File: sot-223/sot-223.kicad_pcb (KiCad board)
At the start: 2 copper layers, 21.6 x 15.2 mm, 2 parts, among them J1 Conn_01x04, J2 Conn_01x04_Male

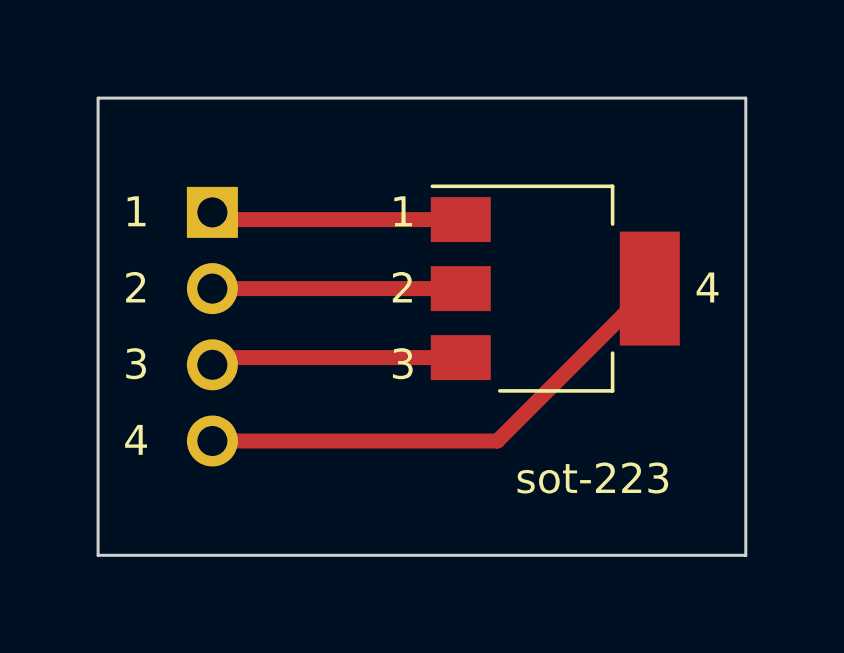
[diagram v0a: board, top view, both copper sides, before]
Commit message: Add zones to SOT-223 PCB
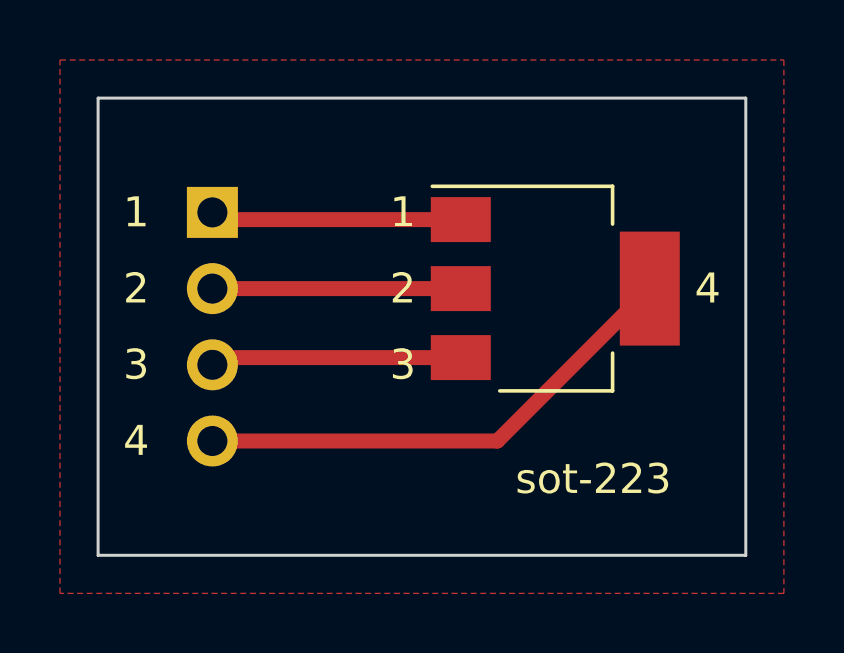
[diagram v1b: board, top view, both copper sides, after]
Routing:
- added copper zone on F.Cu, net (none)
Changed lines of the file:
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@@
       (effects (font (size 1 1) (thickness 0.15)) (justify mirror))
     )
+    (fp_line (start 1.8 1.8) (end -1.8 1.8) (layer B.CrtYd) (width 0.05))
+    (fp_line (start 1.8 -9.4) (end 1.8 1.8) (layer B.CrtYd) (width 0.05))
+    (fp_line (start -1.8 -9.4) (end 1.8 -9.4) (layer B.CrtYd) (width 0.05))
+    (fp_line (start -1.8 1.8) (end -1.8 -9.4) (layer B.CrtYd) (width 0.05))
+    (fp_line (start -1.33 1.33) (end 0 1.33) (layer B.SilkS) (width 0.12))
+    (fp_line (start -1.33 0) (end -1.33 1.33) (layer B.SilkS) (width 0.12))
+    (fp_line (start -1.33 -1.27) (end 1.33 -1.27) (layer B.SilkS) (width 0.12))
+    (fp_line (start 1.33 -1.27) (end 1.33 -8.95) (layer B.SilkS) (width 0.12))
+    (fp_line (start -1.33 -1.27) (end -1.33 -8.95) (layer B.SilkS) (width 0.12))
+    (fp_line (start -1.33 -8.95) (end 1.33 -8.95) (layer B.SilkS) (width 0.12))
+    (fp_line (start -1.27 0.635) (end -0.635 1.27) (layer B.Fab) (width 0.1))
+    (fp_line (start -1.27 -8.89) (end -1.27 0.635) (layer B.Fab) (width 0.1))
+    (fp_line (start 1.27 -8.89) (end -1.27 -8.89) (layer B.Fab) (width 0.1))
+    (fp_line (start 1.27 1.27) (end 1.27 -8.89) (layer B.Fab) (width 0.1))
+    (fp_line (start -0.635 1.27) (end 1.27 1.27) (layer B.Fab) (width 0.1))
     (fp_text user %R (at 0 -3.81 270) (layer B.Fab)
       (effects (font (size 1 1) (thickness 0.15)) (justify mirror))
     )
-    (fp_line (start -0.635 1.27) (end 1.27 1.27) (layer B.Fab) (width 0.1))
-    (fp_line (start 1.27 1.27) (end 1.27 -8.89) (layer B.Fab) (width 0.1))
-    (fp_line (start 1.27 -8.89) (end -1.27 -8.89) (layer B.Fab) (width 0.1))
-    (fp_line (start -1.27 -8.89) (end -1.27 0.635) (layer B.Fab) (width 0.1))
-    (fp_line (start -1.27 0.635) (end -0.635 1.27) (layer B.Fab) (width 0.1))
-    (fp_line (start -1.33 -8.95) (end 1.33 -8.95) (layer B.SilkS) (width 0.12))
-    (fp_line (start -1.33 -1.27) (end -1.33 -8.95) (layer B.SilkS) (width 0.12))
-    (fp_line (start 1.33 -1.27) (end 1.33 -8.95) (layer B.SilkS) (width 0.12))
-    (fp_line (start -1.33 -1.27) (end 1.33 -1.27) (layer B.SilkS) (width 0.12))
-    (fp_line (start -1.33 0) (end -1.33 1.33) (layer B.SilkS) (width 0.12))
-    (fp_line (start -1.33 1.33) (end 0 1.33) (layer B.SilkS) (width 0.12))
-    (fp_line (start -1.8 1.8) (end -1.8 -9.4) (layer B.CrtYd) (width 0.05))
-    (fp_line (start -1.8 -9.4) (end 1.8 -9.4) (layer B.CrtYd) (width 0.05))
-    (fp_line (start 1.8 -9.4) (end 1.8 1.8) (layer B.CrtYd) (width 0.05))
-    (fp_line (start 1.8 1.8) (end -1.8 1.8) (layer B.CrtYd) (width 0.05))
     (pad 4 thru_hole oval (at 0 -7.62 180) (size 1.7 1.7) (drill 1) (layers *.Cu *.Mask)
       (net 4 "Net-(J1-Pad4)"))
@@
       (effects (font (size 1 1) (thickness 0.15)))
     )
+    (fp_line (start 1.85 -3.35) (end 1.85 3.35) (layer F.Fab) (width 0.1))
+    (fp_line (start -1.85 3.35) (end 1.85 3.35) (layer F.Fab) (width 0.1))
+    (fp_line (start -4.1 -3.41) (end 1.91 -3.41) (layer F.SilkS) (width 0.12))
+    (fp_line (start -0.8 -3.35) (end 1.85 -3.35) (layer F.Fab) (width 0.1))
+    (fp_line (start -1.85 3.41) (end 1.91 3.41) (layer F.SilkS) (width 0.12))
+    (fp_line (start -1.85 -2.3) (end -1.85 3.35) (layer F.Fab) (width 0.1))
+    (fp_line (start -4.4 -3.6) (end -4.4 3.6) (layer F.CrtYd) (width 0.05))
+    (fp_line (start -4.4 3.6) (end 4.4 3.6) (layer F.CrtYd) (width 0.05))
+    (fp_line (start 4.4 3.6) (end 4.4 -3.6) (layer F.CrtYd) (width 0.05))
+    (fp_line (start 4.4 -3.6) (end -4.4 -3.6) (layer F.CrtYd) (width 0.05))
+    (fp_line (start 1.91 -3.41) (end 1.91 -2.15) (layer F.SilkS) (width 0.12))
+    (fp_line (start 1.91 3.41) (end 1.91 2.15) (layer F.SilkS) (width 0.12))
+    (fp_line (start -1.85 -2.3) (end -0.8 -3.35) (layer F.Fab) (width 0.1))
     (fp_text user %R (at 0 0 90) (layer F.Fab)
       (effects (font (size 0.8 0.8) (thickness 0.12)))
     )
-    (fp_line (start -1.85 -2.3) (end -0.8 -3.35) (layer F.Fab) (width 0.1))
-    (fp_line (start 1.91 3.41) (end 1.91 2.15) (layer F.SilkS) (width 0.12))
-    (fp_line (start 1.91 -3.41) (end 1.91 -2.15) (layer F.SilkS) (width 0.12))
-    (fp_line (start 4.4 -3.6) (end -4.4 -3.6) (layer F.CrtYd) (width 0.05))
-    (fp_line (start 4.4 3.6) (end 4.4 -3.6) (layer F.CrtYd) (width 0.05))
-    (fp_line (start -4.4 3.6) (end 4.4 3.6) (layer F.CrtYd) (width 0.05))
-    (fp_line (start -4.4 -3.6) (end -4.4 3.6) (layer F.CrtYd) (width 0.05))
-    (fp_line (start -1.85 -2.3) (end -1.85 3.35) (layer F.Fab) (width 0.1))
-    (fp_line (start -1.85 3.41) (end 1.91 3.41) (layer F.SilkS) (width 0.12))
-    (fp_line (start -0.8 -3.35) (end 1.85 -3.35) (layer F.Fab) (width 0.1))
-    (fp_line (start -4.1 -3.41) (end 1.91 -3.41) (layer F.SilkS) (width 0.12))
-    (fp_line (start -1.85 3.35) (end 1.85 3.35) (layer F.Fab) (width 0.1))
-    (fp_line (start 1.85 -3.35) (end 1.85 3.35) (layer F.Fab) (width 0.1))
     (pad 1 smd rect (at -3.15 -2.3) (size 2 1.5) (layers F.Cu F.Paste F.Mask)
       (net 1 "Net-(J1-Pad1)"))
@@
   (segment (start 150.47 96.52) (end 140.97 96.52) (width 0.5) (layer F.Cu) (net 4))
   (segment (start 155.55 91.44) (end 150.47 96.52) (width 0.5) (layer F.Cu) (net 4))
+  (zone (net 0) (net_name "") (layer F.Cu) (hatch edge 0.508)
+    (connect_pads (clearance 0.508))
+    (min_thickness 0.254)
+    (fill yes (arc_segments 32) (thermal_gap 0.508) (thermal_bridge_width 0.508))
+    (polygon
+      (pts
+        (xy 160.02 101.6) (xy 135.89 101.6) (xy 135.89 83.82) (xy 160.02 83.82)
+      )
+    )
+  )
 )
